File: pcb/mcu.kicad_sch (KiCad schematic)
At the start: 22 parts, among them U1 ATtiny1616-MNR

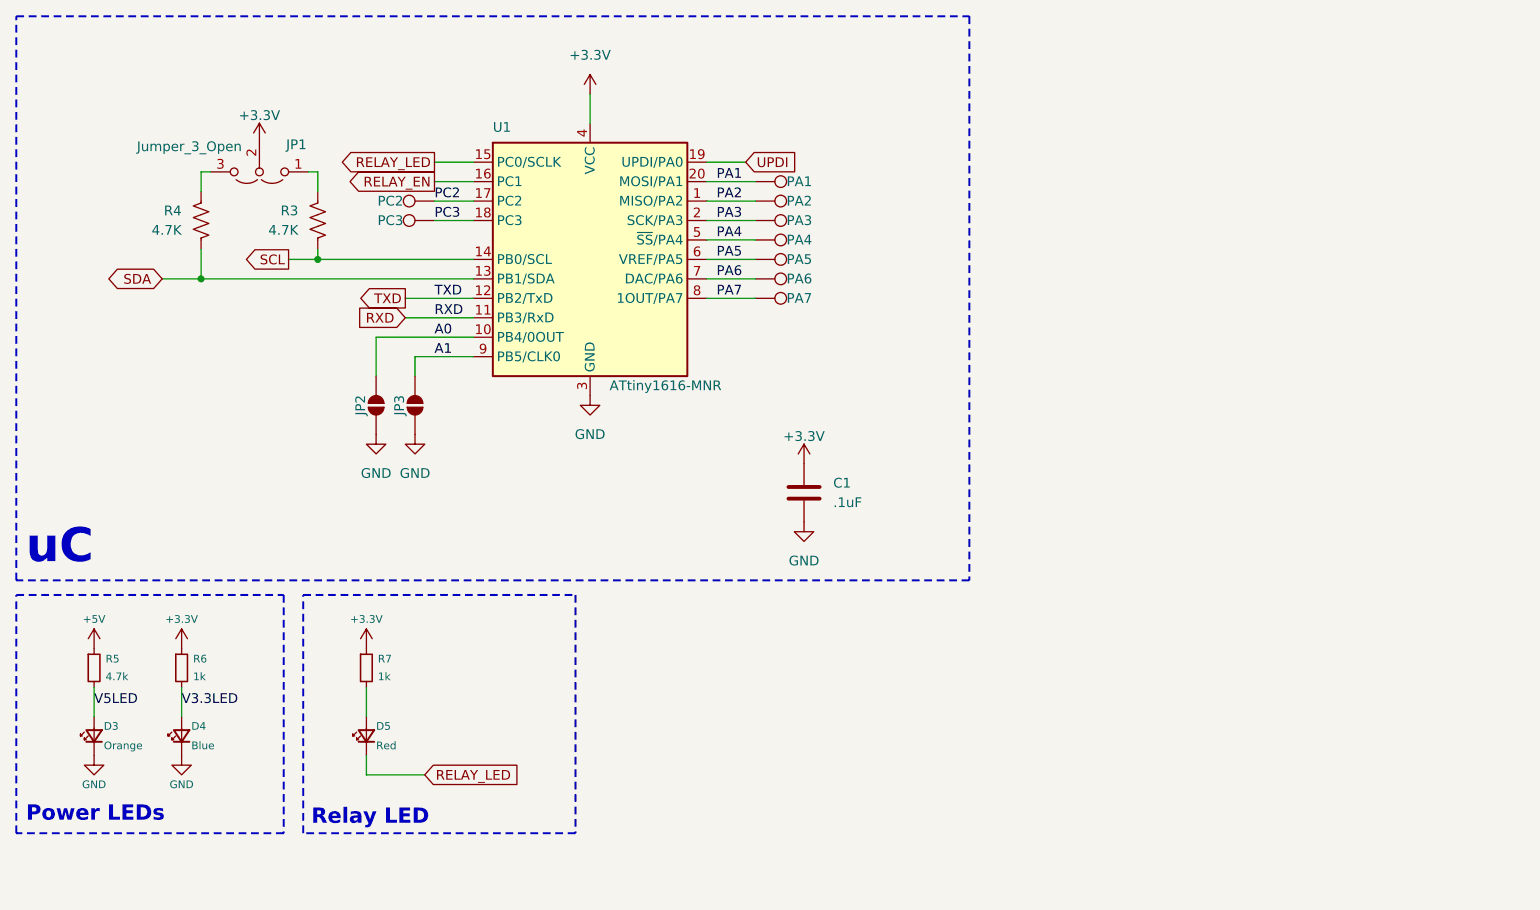
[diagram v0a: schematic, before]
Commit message: Updated to latest libraries
Changed to all CRG footprints (mostly)
Moved somethings around
Added LED jumper
Updated symbols/logos
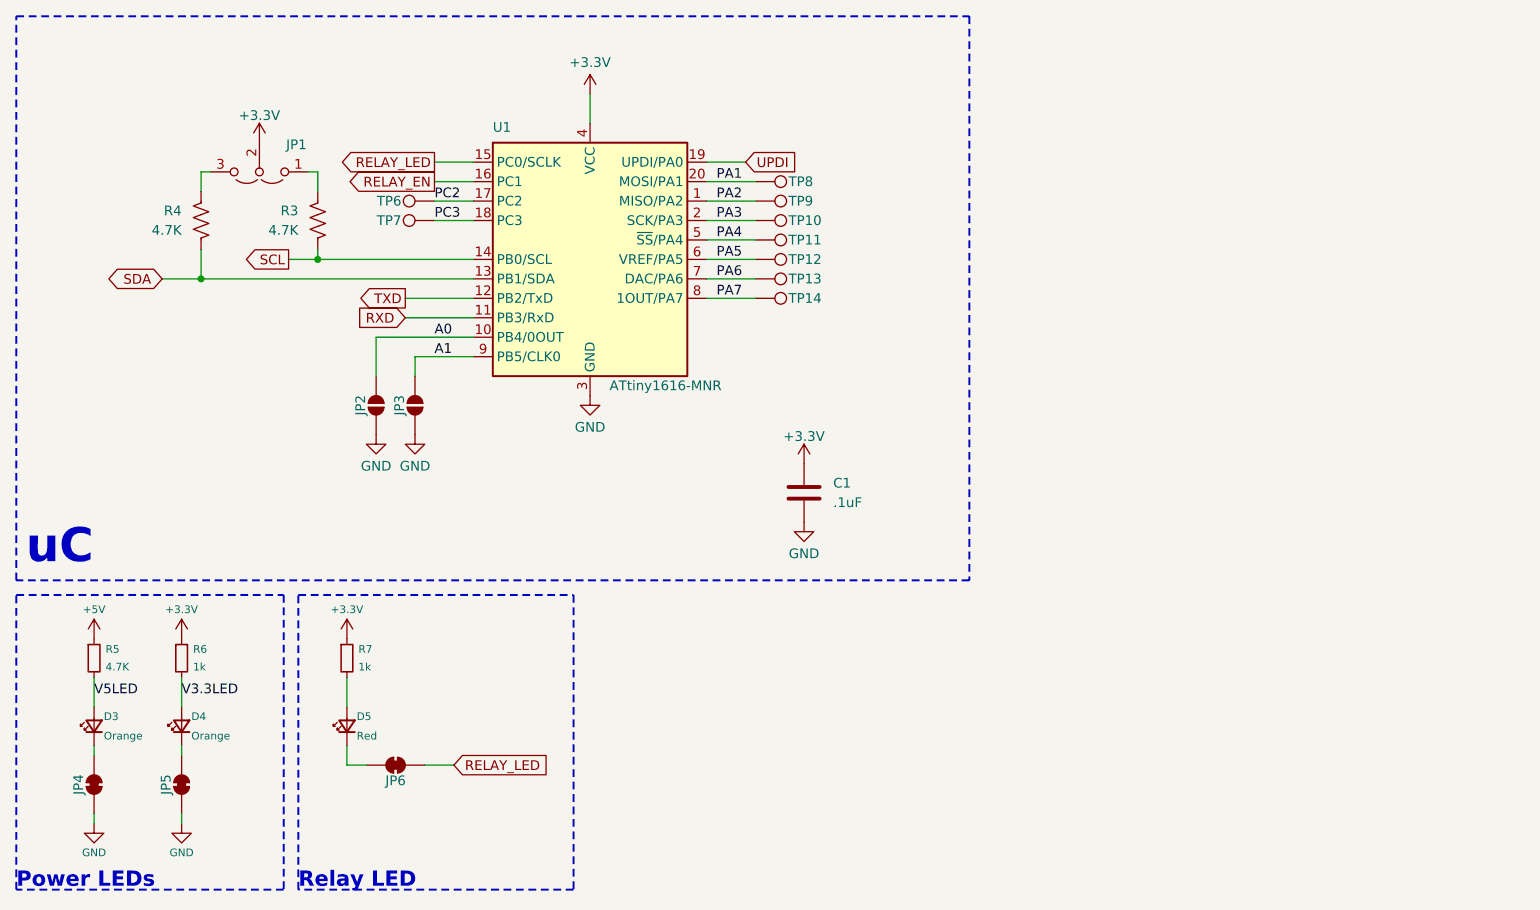
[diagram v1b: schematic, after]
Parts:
- added JP4, JP5, JP6: ~, CRGM Connector:SolderJumper-2_P1.3mm_Bridged_RoundedPad1.0x1.5mm, symbol CRGM Connector:SolderJumper_2_Bridged
- C1: footprint Capacitor_SMD:C_0603_1608Metric -> CRGM Passive:C_0603_1608Metric; Digikey (none) -> 1276-1860-2-ND; Mouser (none) -> 187-CL10A105KB8NNNC
- D3, D5: footprint LED_SMD:LED_0603_1608Metric -> CRGM Passive:LED_0603_1608Metric
- D4: value Blue -> Orange; footprint LED_SMD:LED_0603_1608Metric -> CRGM Passive:LED_0603_1608Metric; Digikey 5962-XL-1608UBC-04TR-ND -> 5962-XL-1608UOC-06TR-ND; LCSC C965807 -> C965800; MPN XL-1608UBC-04 -> XL-1608UOC-06; Mouser 710-150060BS75020 -> 859-LTST-C190KFKT
- JP1: value Jumper_3_Open -> ~
- JP2: value A0 -> ~
- JP3: value A1 -> ~
- R3, R4, R6, R7: footprint Resistor_SMD:R_0603_1608Metric -> CRGM Passive:R_0603_1608Metric
- R5: value 4.7k -> 4.7K; footprint Resistor_SMD:R_0603_1608Metric -> CRGM Passive:R_0603_1608Metric
- TP10: value PA3 -> ~; symbol Connector:TestPoint -> CRGM Connector:TestPoint
- TP11: value PA4 -> ~; symbol Connector:TestPoint -> CRGM Connector:TestPoint
- TP12: value PA5 -> ~; symbol Connector:TestPoint -> CRGM Connector:TestPoint
- TP13: value PA6 -> ~; symbol Connector:TestPoint -> CRGM Connector:TestPoint
- TP14: value PA7 -> ~; symbol Connector:TestPoint -> CRGM Connector:TestPoint
- TP6: value PC2 -> ~; symbol Connector:TestPoint -> CRGM Connector:TestPoint
- TP7: value PC3 -> ~; symbol Connector:TestPoint -> CRGM Connector:TestPoint
- TP8: value PA1 -> ~; symbol Connector:TestPoint -> CRGM Connector:TestPoint
- TP9: value PA2 -> ~; symbol Connector:TestPoint -> CRGM Connector:TestPoint
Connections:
- net GND: now also JP4.1 (A), JP5.1 (A); no longer D3.1 (K), D4.1 (K)
- net RELAY_LED: now also JP6.1 (A); no longer D5.1 (K)
- new net: D4.1 (K), JP5.2 (B)
- new net: D3.1 (K), JP4.2 (B)
- new net: D5.1 (K), JP6.2 (B)
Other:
- moved on the sheet: D3, D4, D5, R5, R6, R7

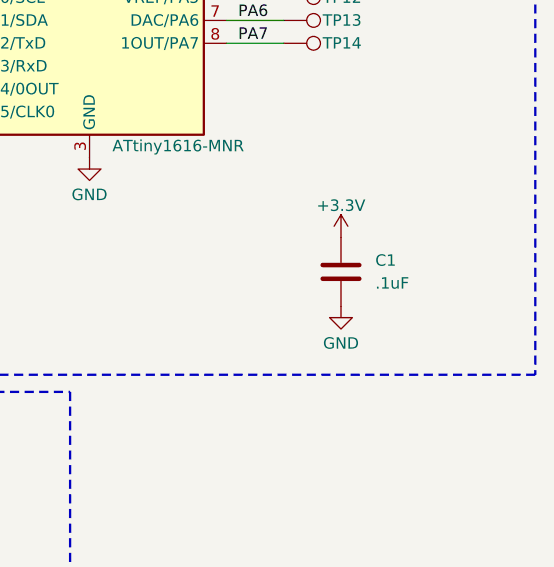
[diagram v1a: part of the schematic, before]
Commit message: Fixed capacitor attributes
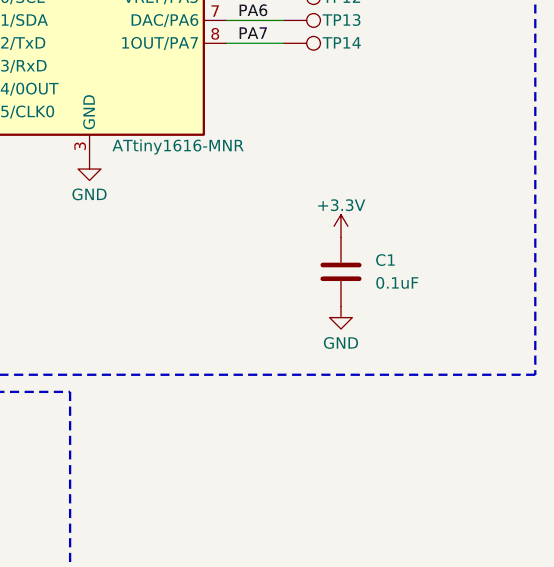
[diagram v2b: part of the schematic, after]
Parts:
- C1: value .1uF -> 0.1uF; Digikey 1276-1860-2-ND -> 1276-1005-2-ND; LCSC C15849 -> C66501; MPN CL10A105KB8NNNC -> CL10B104KO8NNNC; Mouser 187-CL10A105KB8NNNC -> 187-CL10B104KO8NNNC; Tolerance (none) -> 10%; Vr (none) -> 16V
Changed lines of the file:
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@@
-			)
-		)
-		(property "Sim.Enable" ""
-			(at 40.64 102.87 0)
-			(effects
-				(font
-					(size 1.27 1.27)
-				)
-				(hide yes)
 			)
 		)
@@
 			)
 		)
-		(property "Sim.Enable" ""
-			(at 66.04 69.85 0)
-			(effects
-				(font
-					(size 1.27 1.27)
-				)
-				(hide yes)
-			)
-		)
 		(pin "1"
 		)
@@
 			)
 		)
-		(property "Sim.Enable" ""
-			(at 73.66 45.72 90)
-			(effects
-				(font
-					(size 1.27 1.27)
-				)
-				(hide yes)
-			)
-		)
 		(pin "1"
 		)
@@
 			)
 		)
-		(property "Sim.Enable" ""
-			(at 115.57 50.8 90)
-			(effects
-				(font
-					(size 1.27 1.27)
-				)
-				(hide yes)
-			)
-		)
 		(pin "1"
 		)
@@
 			)
 		)
-		(property "Sim.Enable" ""
-			(at 40.64 111.76 90)
-			(effects
-				(font
-					(size 1.27 1.27)
-				)
-				(hide yes)
-			)
-		)
 		(property "Sim.Pin" "1=K 2=A"
 			(at 40.64 111.76 0)
@@
 			)
 		)
-		(property "Sim.Enable" ""
-			(at 73.66 43.18 90)
-			(effects
-				(font
-					(size 1.27 1.27)
-				)
-				(hide yes)
-			)
-		)
 		(pin "1"
 		)
@@
 		(property "Description" "Solder Jumper, 2-pole, closed/bridged"
 			(at 36.322 119.38 0)
-			(effects
-				(font
-					(size 1.27 1.27)
-				)
-				(hide yes)
-			)
-		)
-		(property "Sim.Enable" ""
-			(at 29.21 119.38 0)
 			(effects
 				(font
@@
 			)
 		)
-		(property "Value" ".1uF"
+		(property "Value" "0.1uF"
 			(at 125.73 82.5499 0)
 			(effects
@@
 			)
 		)
-		(property "MPN" "CL10A105KB8NNNC"
+		(property "MPN" "CL10B104KO8NNNC"
 			(at 121.92 81.28 0)
 			(effects
@@
 			)
 		)
-		(property "LCSC" "C15849"
+		(property "LCSC" "C66501"
 			(at 121.92 81.28 0)
 			(effects
@@
 			)
 		)
-		(property "Digikey" "1276-1860-2-ND"
+		(property "Digikey" "1276-1005-2-ND"
 			(at 121.92 81.28 0)
 			(effects
@@
 			)
 		)
-		(property "Mouser" "187-CL10A105KB8NNNC"
+		(property "Mouser" "187-CL10B104KO8NNNC"
 			(at 121.92 81.28 0)
 			(effects
@@
 			)
 		)
-		(property "Sim.Enable" ""
+		(property "Tolerance" "10%"
+			(at 121.92 81.28 0)
+			(effects
+				(font
+					(size 1.27 1.27)
+				)
+				(hide yes)
+			)
+		)
+		(property "Vr" "16V"
 			(at 121.92 81.28 0)
 			(effects
@@
 			)
 		)
-		(property "Sim.Enable" ""
-			(at 58.42 45.72 0)
-			(effects
-				(font
-					(size 1.27 1.27)
-				)
-				(hide yes)
-			)
-		)
 		(pin "2"
 		)
@@
 			)
 		)
-		(property "Sim.Enable" ""
-			(at 50.8 39.37 0)
-			(effects
-				(font
-					(size 1.27 1.27)
-				)
-				(hide yes)
-			)
-		)
 		(pin "3"
 		)
@@
 		(property "Description" "Solder Jumper, 2-pole, closed/bridged"
 			(at 68.58 109.728 0)
-			(effects
-				(font
-					(size 1.27 1.27)
-				)
-				(hide yes)
-			)
-		)
-		(property "Sim.Enable" ""
-			(at 68.58 116.84 0)
 			(effects
 				(font
@@
 			)
 		)
-		(property "Sim.Enable" ""
-			(at 115.57 40.64 90)
-			(effects
-				(font
-					(size 1.27 1.27)
-				)
-				(hide yes)
-			)
-		)
 		(pin "1"
 		)
@@
 			)
 		)
-		(property "Sim.Enable" ""
-			(at 43.18 45.72 0)
-			(effects
-				(font
-					(size 1.27 1.27)
-				)
-				(hide yes)
-			)
-		)
 		(pin "2"
 		)
@@
 			)
 		)
-		(property "Sim.Enable" ""
-			(at 62.23 102.87 0)
-			(effects
-				(font
-					(size 1.27 1.27)
-				)
-				(hide yes)
-			)
-		)
 		(pin "1"
 		)
@@
 			)
 		)
-		(property "Sim.Enable" ""
-			(at 29.21 102.87 0)
-			(effects
-				(font
-					(size 1.27 1.27)
-				)
-				(hide yes)
-			)
-		)
 		(pin "1"
 		)
@@
 			)
 		)
-		(property "Sim.Enable" ""
-			(at 115.57 43.18 90)
-			(effects
-				(font
-					(size 1.27 1.27)
-				)
-				(hide yes)
-			)
-		)
 		(pin "1"
 		)
@@
 			)
 		)
-		(property "Sim.Enable" ""
-			(at 29.21 111.76 90)
-			(effects
-				(font
-					(size 1.27 1.27)
-				)
-				(hide yes)
-			)
-		)
 		(property "Sim.Pin" "1=K 2=A"
 			(at 29.21 111.76 0)
@@
 		(property "Description" "Test Point D1.0mm"
 			(at 106.426 48.26 0)
-			(effects
-				(font
-					(size 1.27 1.27)
-				)
-				(hide yes)
-			)
-		)
-		(property "Sim.Enable" ""
-			(at 115.57 48.26 90)
 			(effects
 				(font
@@
 			)
 		)
-		(property "Sim.Enable" ""
-			(at 115.57 55.88 90)
-			(effects
-				(font
-					(size 1.27 1.27)
-				)
-				(hide yes)
-			)
-		)
 		(pin "1"
 		)
@@
 			)
 		)
-		(property "Sim.Enable" ""
-			(at 115.57 45.72 90)
-			(effects
-				(font
-					(size 1.27 1.27)
-				)
-				(hide yes)
-			)
-		)
 		(pin "1"
 		)
@@
 			)
 		)
-		(property "Sim.Enable" ""
-			(at 115.57 53.34 90)
-			(effects
-				(font
-					(size 1.27 1.27)
-				)
-				(hide yes)
-			)
-		)
 		(pin "1"
 		)
@@
 			)
 		)
-		(property "Sim.Enable" ""
-			(at 40.64 119.38 0)
-			(effects
-				(font
-					(size 1.27 1.27)
-				)
-				(hide yes)
-			)
-		)
 		(pin "2"
 		)
@@
 			)
 		)
-		(property "Sim.Enable" ""
-			(at 93.98 55.88 0)
-			(effects
-				(font
-					(size 1.27 1.27)
-				)
-				(hide yes)
-			)
-		)
 		(pin "21"
 		)
@@
 			)
 		)
-		(property "Sim.Enable" ""
-			(at 62.23 111.76 90)
-			(effects
-				(font
-					(size 1.27 1.27)
-				)
-				(hide yes)
-			)
-		)
 		(property "Sim.Pin" "1=K 2=A"
 			(at 62.23 111.76 0)
@@
 			(at 71.12 69.85 0)
 			(effects
-				(font
-					(size 1.27 1.27)
-				)
-				(hide yes)
-			)
-		)
-		(property "Sim.Enable" ""
-			(at 71.12 69.85 0)
-			(effects

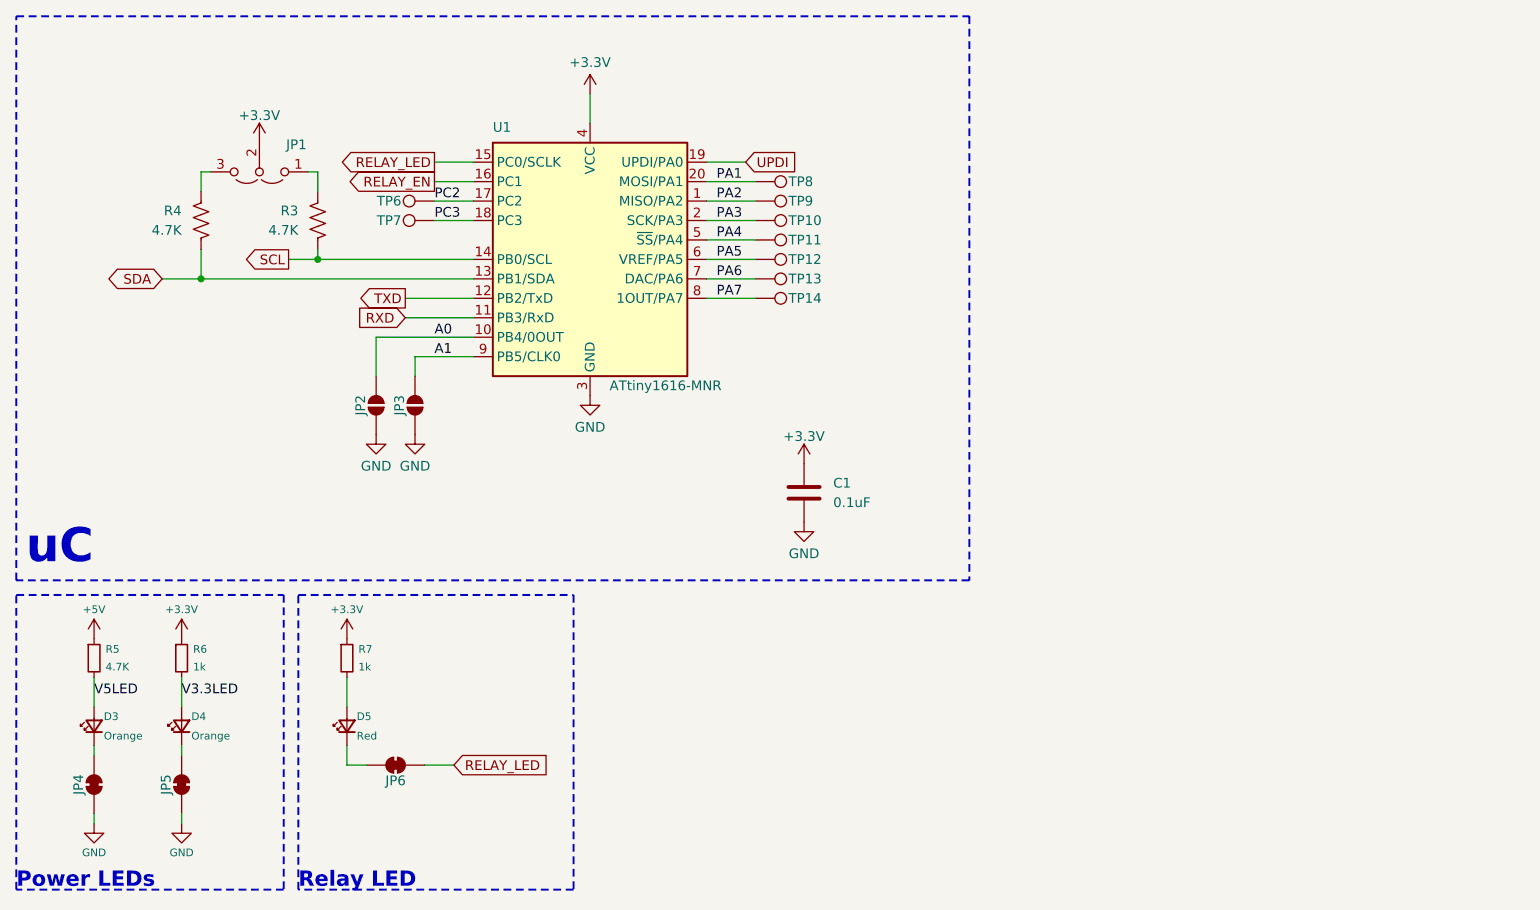
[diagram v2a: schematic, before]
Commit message: Updated for consistency
Updated footprints
Added ESD to power
Added second QWICC connector
Rerouted as required
Made mounting holes grounded
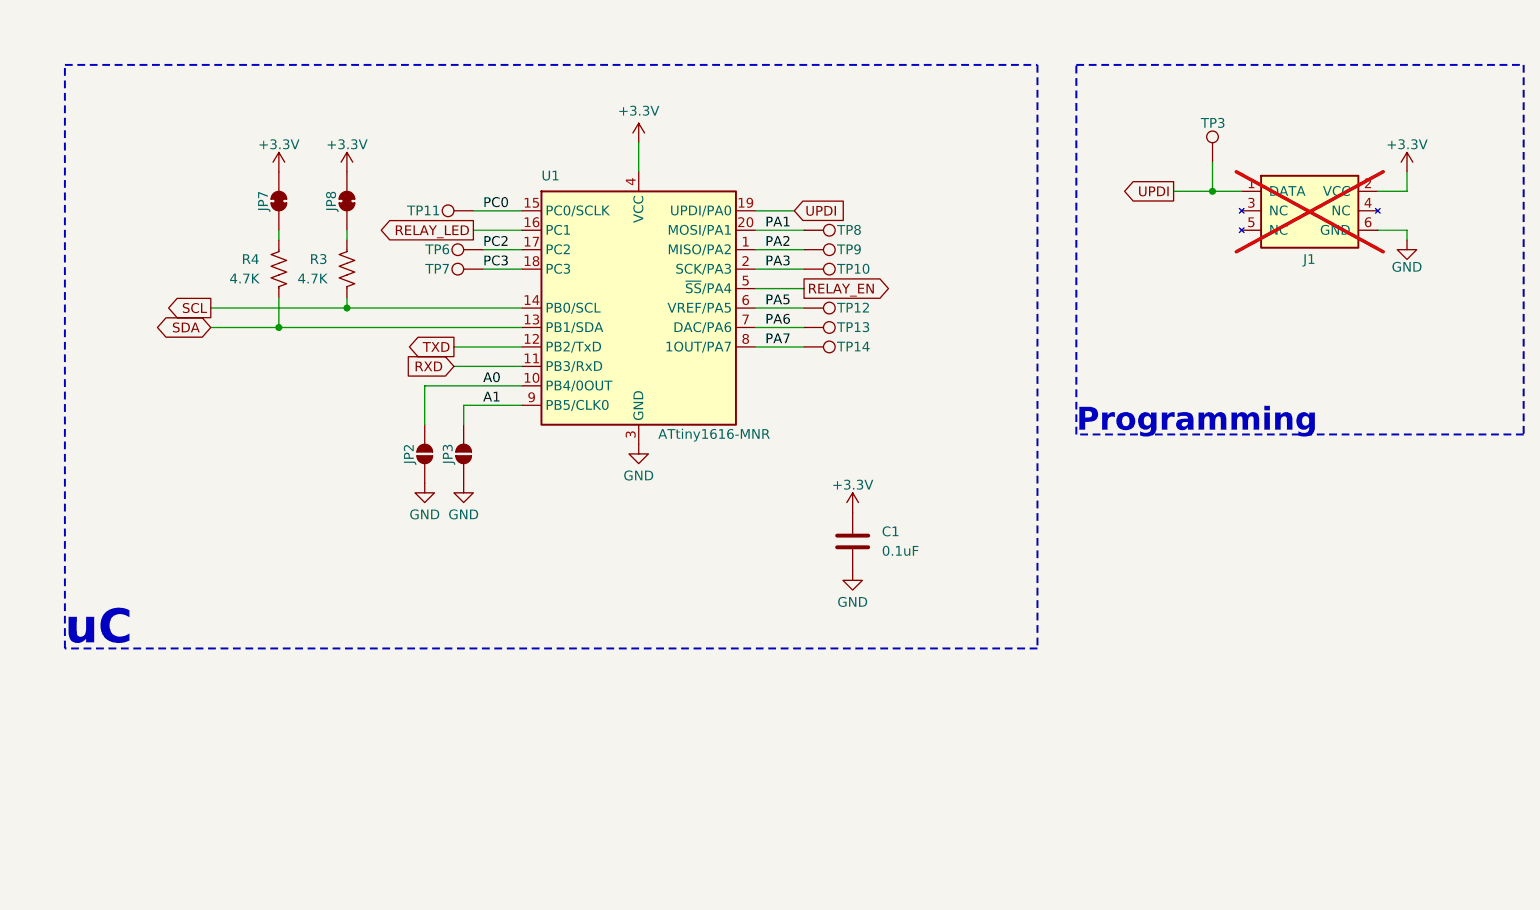
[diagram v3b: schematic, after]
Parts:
- removed D3, D4: Orange, CRGM Passive:LED_0603_1608Metric, symbol Device:LED_Small
- removed D5: Red, CRGM Passive:LED_0603_1608Metric, symbol Device:LED_Small
- removed JP1: ~, CRGM Connector:SolderJumper-3_P1.3mm_Open_RoundedPad1.0x1.5mm, symbol Jumper:Jumper_3_Open
- removed JP4, JP5, JP6: ~, CRGM Connector:SolderJumper-2_P1.3mm_Bridged_RoundedPad1.0x1.5mm, symbol CRGM Connector:SolderJumper_2_Bridged
- removed R5: 4.7K, CRGM Passive:R_0603_1608Metric, symbol Device:R_Small
- removed R6, R7: 1k, CRGM Passive:R_0603_1608Metric, symbol Device:R_Small
- added J1: AVR-UPDI-6, CRGM Connector:PinHeader_2x03_P2.54mm_Vertical_SMD, symbol CRGM Connector:AVR-UPDI-6
- added JP7, JP8: ~, CRGM Connector:SolderJumper-2_P1.3mm_Bridged_RoundedPad1.0x1.5mm, symbol Jumper:SolderJumper_2_Bridged
- added TP3: ~, CRGM Mechanical:TestPoint_Pad_D1.0mm, symbol CRGM Connector:TestPoint
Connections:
- net +3.3V: now also J1.2 (VCC), JP7.2 (B), JP8.2 (B)
- net GND: now also J1.6 (GND)
- net RELAY_EN: now also U1.5 (~{SS}/PA4); no longer U1.16 (PC1)
- net RELAY_LED: now also U1.16 (PC1); no longer U1.15 (PC0/SCLK)
- net UPDI: now also J1.1 (DATA), TP3.1
- net at R3.2: now also JP8.1 (A)
- net at R4.2: now also JP7.1 (A)
- net PA4 renamed PC0
- net PC0: now also U1.15 (PC0/SCLK); no longer U1.5 (~{SS}/PA4)
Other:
- note added: "Programming"
- note removed: "Power LEDs"
- note removed: "Relay LED"
- moved on the sheet: C1, JP2, JP3, R3, R4, TP10, TP11, TP12, TP13, TP14, TP6, TP7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
